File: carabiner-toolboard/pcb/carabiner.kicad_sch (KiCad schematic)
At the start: 24 parts, among them J1 MF-Vertical 43045-1612, J2 MF-Horizontal 43045-1621, J7 MF-Horizontal 43045-1600

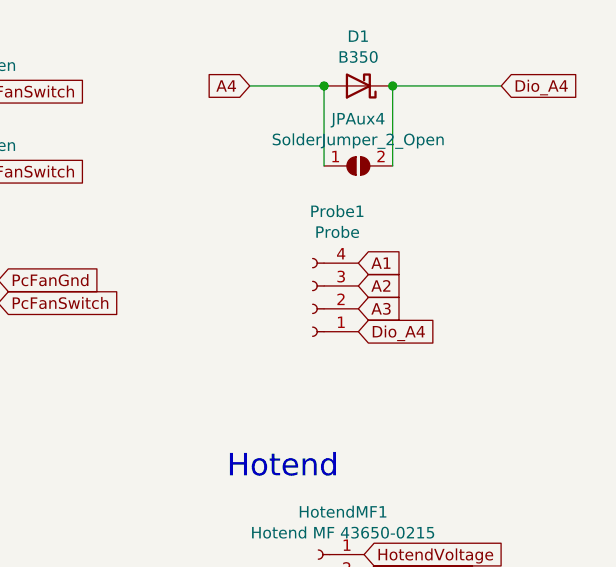
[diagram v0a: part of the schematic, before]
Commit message: Carabiner R1.1 - 'Who even needs more pins?'
Duplicates Aux3 - this allows you to wire up a BLTouch much easier
Increase the maximum ampere for PCFs to 2A total
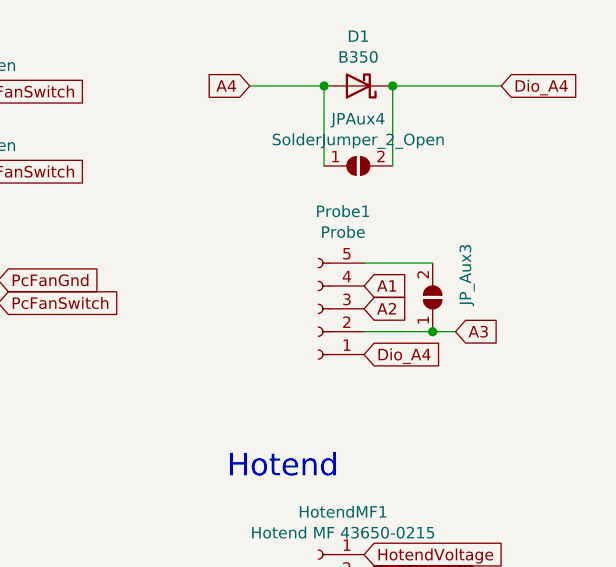
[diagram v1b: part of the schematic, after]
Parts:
- added JP_Aux3: SolderJumper_2_Open, Jumper:SolderJumper-2_P1.3mm_Open_TrianglePad1.0x1.5mm, symbol Jumper:SolderJumper_2_Open
- Probe1: footprint Connector_JST:JST_XH_B4B-XH-A_1x04_P2.50mm_Vertical -> Connector_JST:JST_XH_B5B-XH-A_1x05_P2.50mm_Vertical; symbol Connector:Conn_01x04_Female -> Connector:Conn_01x05_Female
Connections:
- net A3: now also JP_Aux3.1 (A)
- new net: JP_Aux3.2 (B), Probe1.5 (Pin_5)
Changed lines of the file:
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@@
   (junction (at 248.285 34.925) (diameter 1.016) (color 0 0 0 0))
   (junction (at 255.905 34.925) (diameter 1.016) (color 0 0 0 0))
+  (junction (at 260.35 62.23) (diameter 1.016) (color 0 0 0 0))
   (wire (pts (xy 196.85 56.515) (xy 200.66 56.515))
     (stroke (width 0) (type solid) (color 0 0 0 0))
@@
     (stroke (width 0) (type solid) (color 0 0 0 0))
   )
+  (wire (pts (xy 252.73 54.61) (xy 260.35 54.61))
+    (stroke (width 0) (type solid) (color 0 0 0 0))
+  )
+  (wire (pts (xy 252.73 62.23) (xy 260.35 62.23))
+    (stroke (width 0) (type solid) (color 0 0 0 0))
+  )
   (wire (pts (xy 255.905 34.925) (xy 255.905 43.815))
     (stroke (width 0) (type solid) (color 0 0 0 0))
   )
   (wire (pts (xy 255.905 34.925) (xy 267.97 34.925))
+    (stroke (width 0) (type solid) (color 0 0 0 0))
+  )
+  (wire (pts (xy 260.35 62.23) (xy 262.89 62.23))
     (stroke (width 0) (type solid) (color 0 0 0 0))
   )
@@
     )
   )
-  (global_label "A1" (shape input) (at 252.095 54.61 0) (fields_autoplaced)
-    (effects (font (size 1.27 1.27)) (justify left))
-    (property "Intersheet References" "${INTERSHEET_REFS}" (id 0) (at 256.8062 54.5306 0)
+  (global_label "A1" (shape input) (at 252.73 57.15 0) (fields_autoplaced)
+    (effects (font (size 1.27 1.27)) (justify left))
+    (property "Intersheet References" "${INTERSHEET_REFS}" (id 0) (at 257.4412 57.0706 0)
       (effects (font (size 1.27 1.27)) (justify left) hide)
     )
   )
-  (global_label "A2" (shape input) (at 252.095 57.15 0) (fields_autoplaced)
-    (effects (font (size 1.27 1.27)) (justify left))
-    (property "Intersheet References" "${INTERSHEET_REFS}" (id 0) (at 256.8062 57.0706 0)
+  (global_label "A2" (shape input) (at 252.73 59.69 0) (fields_autoplaced)
+    (effects (font (size 1.27 1.27)) (justify left))
+    (property "Intersheet References" "${INTERSHEET_REFS}" (id 0) (at 257.4412 59.6106 0)
       (effects (font (size 1.27 1.27)) (justify left) hide)
     )
   )
-  (global_label "A3" (shape input) (at 252.095 59.69 0) (fields_autoplaced)
-    (effects (font (size 1.27 1.27)) (justify left))
-    (property "Intersheet References" "${INTERSHEET_REFS}" (id 0) (at 256.8062 59.6106 0)
+  (global_label "Dio_A4" (shape input) (at 252.73 64.77 0) (fields_autoplaced)
+    (effects (font (size 1.27 1.27)) (justify left))
+    (property "Intersheet References" "${INTERSHEET_REFS}" (id 0) (at 261.4326 64.6906 0)
       (effects (font (size 1.27 1.27)) (justify left) hide)
     )
   )
-  (global_label "Dio_A4" (shape input) (at 252.095 62.23 0) (fields_autoplaced)
-    (effects (font (size 1.27 1.27)) (justify left))
-    (property "Intersheet References" "${INTERSHEET_REFS}" (id 0) (at 260.7976 62.1506 0)
+  (global_label "HotendVoltage" (shape input) (at 252.73 86.995 0) (fields_autoplaced)
+    (effects (font (size 1.27 1.27)) (justify left))
+    (property "Intersheet References" "${INTERSHEET_REFS}" (id 0) (at 0 0 0)
+      (effects (font (size 1.27 1.27)) hide)
+    )
+  )
+  (global_label "HotendNeg" (shape input) (at 252.73 89.535 0) (fields_autoplaced)
+    (effects (font (size 1.27 1.27)) (justify left))
+    (property "Intersheet References" "${INTERSHEET_REFS}" (id 0) (at 0 0 0)
+      (effects (font (size 1.27 1.27)) hide)
+    )
+  )
+  (global_label "HotendVoltage" (shape input) (at 252.73 99.695 0) (fields_autoplaced)
+    (effects (font (size 1.27 1.27)) (justify left))
+    (property "Intersheet References" "${INTERSHEET_REFS}" (id 0) (at 0 0 0)
+      (effects (font (size 1.27 1.27)) hide)
+    )
+  )
+  (global_label "HotendNeg" (shape input) (at 252.73 102.235 0) (fields_autoplaced)
+    (effects (font (size 1.27 1.27)) (justify left))
+    (property "Intersheet References" "${INTERSHEET_REFS}" (id 0) (at 0 0 0)
+      (effects (font (size 1.27 1.27)) hide)
+    )
+  )
+  (global_label "HotendVoltage" (shape input) (at 252.73 111.125 0) (fields_autoplaced)
+    (effects (font (size 1.27 1.27)) (justify left))
+    (property "Intersheet References" "${INTERSHEET_REFS}" (id 0) (at 0 0 0)
+      (effects (font (size 1.27 1.27)) hide)
+    )
+  )
+  (global_label "HotendNeg" (shape input) (at 252.73 113.665 0) (fields_autoplaced)
+    (effects (font (size 1.27 1.27)) (justify left))
+    (property "Intersheet References" "${INTERSHEET_REFS}" (id 0) (at 0 0 0)
+      (effects (font (size 1.27 1.27)) hide)
+    )
+  )
+  (global_label "A3" (shape input) (at 262.89 62.23 0) (fields_autoplaced)
+    (effects (font (size 1.27 1.27)) (justify left))
+    (property "Intersheet References" "${INTERSHEET_REFS}" (id 0) (at 267.6012 62.1506 0)
       (effects (font (size 1.27 1.27)) (justify left) hide)
-    )
-  )
-  (global_label "HotendVoltage" (shape input) (at 252.73 86.995 0) (fields_autoplaced)
-    (effects (font (size 1.27 1.27)) (justify left))
-    (property "Intersheet References" "${INTERSHEET_REFS}" (id 0) (at 0 0 0)
-      (effects (font (size 1.27 1.27)) hide)
-    )
-  )
-  (global_label "HotendNeg" (shape input) (at 252.73 89.535 0) (fields_autoplaced)
-    (effects (font (size 1.27 1.27)) (justify left))
-    (property "Intersheet References" "${INTERSHEET_REFS}" (id 0) (at 0 0 0)
-      (effects (font (size 1.27 1.27)) hide)
-    )
-  )
-  (global_label "HotendVoltage" (shape input) (at 252.73 99.695 0) (fields_autoplaced)
-    (effects (font (size 1.27 1.27)) (justify left))
-    (property "Intersheet References" "${INTERSHEET_REFS}" (id 0) (at 0 0 0)
-      (effects (font (size 1.27 1.27)) hide)
-    )
-  )
-  (global_label "HotendNeg" (shape input) (at 252.73 102.235 0) (fields_autoplaced)
-    (effects (font (size 1.27 1.27)) (justify left))
-    (property "Intersheet References" "${INTERSHEET_REFS}" (id 0) (at 0 0 0)
-      (effects (font (size 1.27 1.27)) hide)
-    )
-  )
-  (global_label "HotendVoltage" (shape input) (at 252.73 111.125 0) (fields_autoplaced)
-    (effects (font (size 1.27 1.27)) (justify left))
-    (property "Intersheet References" "${INTERSHEET_REFS}" (id 0) (at 0 0 0)
-      (effects (font (size 1.27 1.27)) hide)
-    )
-  )
-  (global_label "HotendNeg" (shape input) (at 252.73 113.665 0) (fields_autoplaced)
-    (effects (font (size 1.27 1.27)) (justify left))
-    (property "Intersheet References" "${INTERSHEET_REFS}" (id 0) (at 0 0 0)
-      (effects (font (size 1.27 1.27)) hide)
     )
   )
@@
     (pin "2")
   )
+  (symbol (lib_id "Jumper:SolderJumper_2_Open") (at 260.35 58.42 90) (unit 1)
+    (in_bom yes) (on_board yes)
+    (property "Reference" "JP_Aux3" (id 0) (at 264.033 55.88 0))
+    (property "Value" "SolderJumper_2_Open" (id 1) (at 257.4544 58.42 0)
+      (effects (font (size 1.27 1.27)) hide)
+    )
+    (property "Footprint" "Jumper:SolderJumper-2_P1.3mm_Open_TrianglePad1.0x1.5mm" (id 2) (at 260.35 58.42 0)
+      (effects (font (size 1.27 1.27)) hide)
+    )
+    (property "Datasheet" "~" (id 3) (at 260.35 58.42 0)
+      (effects (font (size 1.27 1.27)) hide)
+    )
+    (pin "1")
+    (pin "2")
+  )
   (symbol (lib_id "Connector:Conn_01x02_Female") (at 47.625 37.465 180) (unit 1)
     (in_bom yes) (on_board yes)
@@
     (pin "4")
   )
-  (symbol (lib_id "Connector:Conn_01x04_Female") (at 247.015 59.69 180) (unit 1)
-    (in_bom yes) (on_board yes)
-    (property "Reference" "Probe1" (id 0) (at 249.7582 48.895 0))
-    (property "Value" "Probe" (id 1) (at 249.7582 51.2064 0))
-    (property "Footprint" "Connector_JST:JST_XH_B4B-XH-A_1x04_P2.50mm_Vertical" (id 2) (at 247.015 59.69 0)
-      (effects (font (size 1.27 1.27)) hide)
-    )
-    (property "Datasheet" "~" (id 3) (at 247.015 59.69 0)
+  (symbol (lib_id "Connector:Conn_01x05_Female") (at 247.65 59.69 180) (unit 1)
+    (in_bom yes) (on_board yes)
+    (property "Reference" "Probe1" (id 0) (at 250.3932 48.895 0))
+    (property "Value" "Probe" (id 1) (at 250.3932 51.2064 0))
+    (property "Footprint" "Connector_JST:JST_XH_B5B-XH-A_1x05_P2.50mm_Vertical" (id 2) (at 247.65 59.69 0)
+      (effects (font (size 1.27 1.27)) hide)
+    )
+    (property "Datasheet" "~" (id 3) (at 247.65 59.69 0)
       (effects (font (size 1.27 1.27)) hide)
     )
@@
     (pin "3")
     (pin "4")
+    (pin "5")
   )
   (symbol (lib_id "Graphic:Logo_Open_Hardware_Small") (at 151.13 99.06 0) (unit 1)
@@
       (reference "JPAux4") (unit 1) (value "SolderJumper_2_Open") (footprint "Jumper:SolderJumper-2_P1.3mm_Open_TrianglePad1.0x1.5mm")
     )
+    (path "/5ccb0dab-e449-450f-be0b-c1fca9d3638a"
+      (reference "JP_Aux3") (unit 1) (value "SolderJumper_2_Open") (footprint "Jumper:SolderJumper-2_P1.3mm_Open_TrianglePad1.0x1.5mm")
+    )
     (path "/00000000-0000-0000-0000-00005ff3998e"
       (reference "JP_HEF_Alt1") (unit 1) (value "SolderJumper_2_Open") (footprint "Jumper:SolderJumper-2_P1.3mm_Open_TrianglePad1.0x1.5mm")
@@
     )
     (path "/00000000-0000-0000-0000-00005ee118e3"
-      (reference "Probe1") (unit 1) (value "Probe") (footprint "Connector_JST:JST_XH_B4B-XH-A_1x04_P2.50mm_Vertical")
+      (reference "Probe1") (unit 1) (value "Probe") (footprint "Connector_JST:JST_XH_B5B-XH-A_1x05_P2.50mm_Vertical")
     )
     (path "/00000000-0000-0000-0000-00005ee148c5"

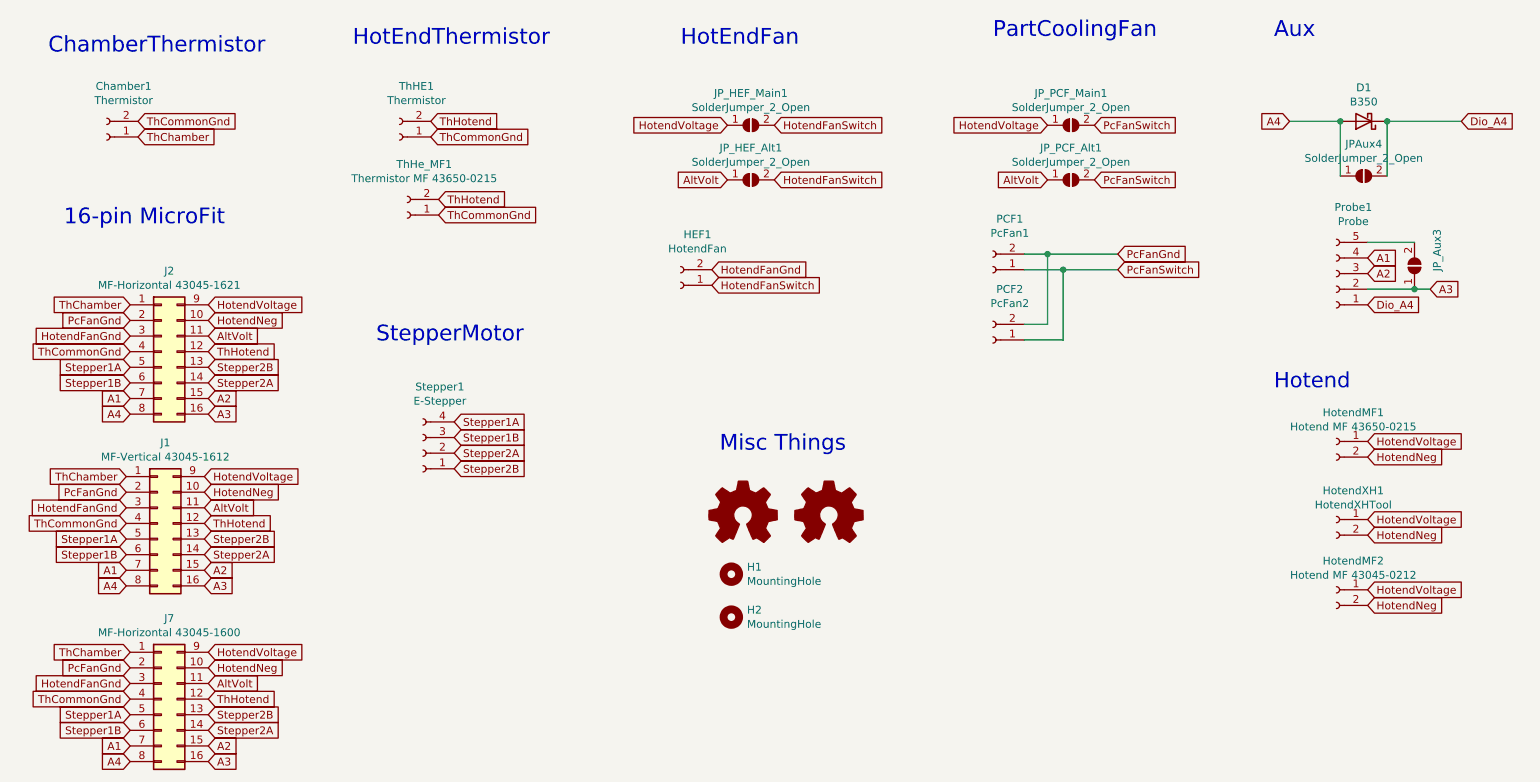
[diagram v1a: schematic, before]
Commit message: Carabiner R 1.2 - Polishing it
- Renaming ports to fit the new unified naming scheme.
- Updated Readme to reflect that
- Support USB with the Aux ports! Use A2 and A3 for D+/D-
- Rework the motor trace routing
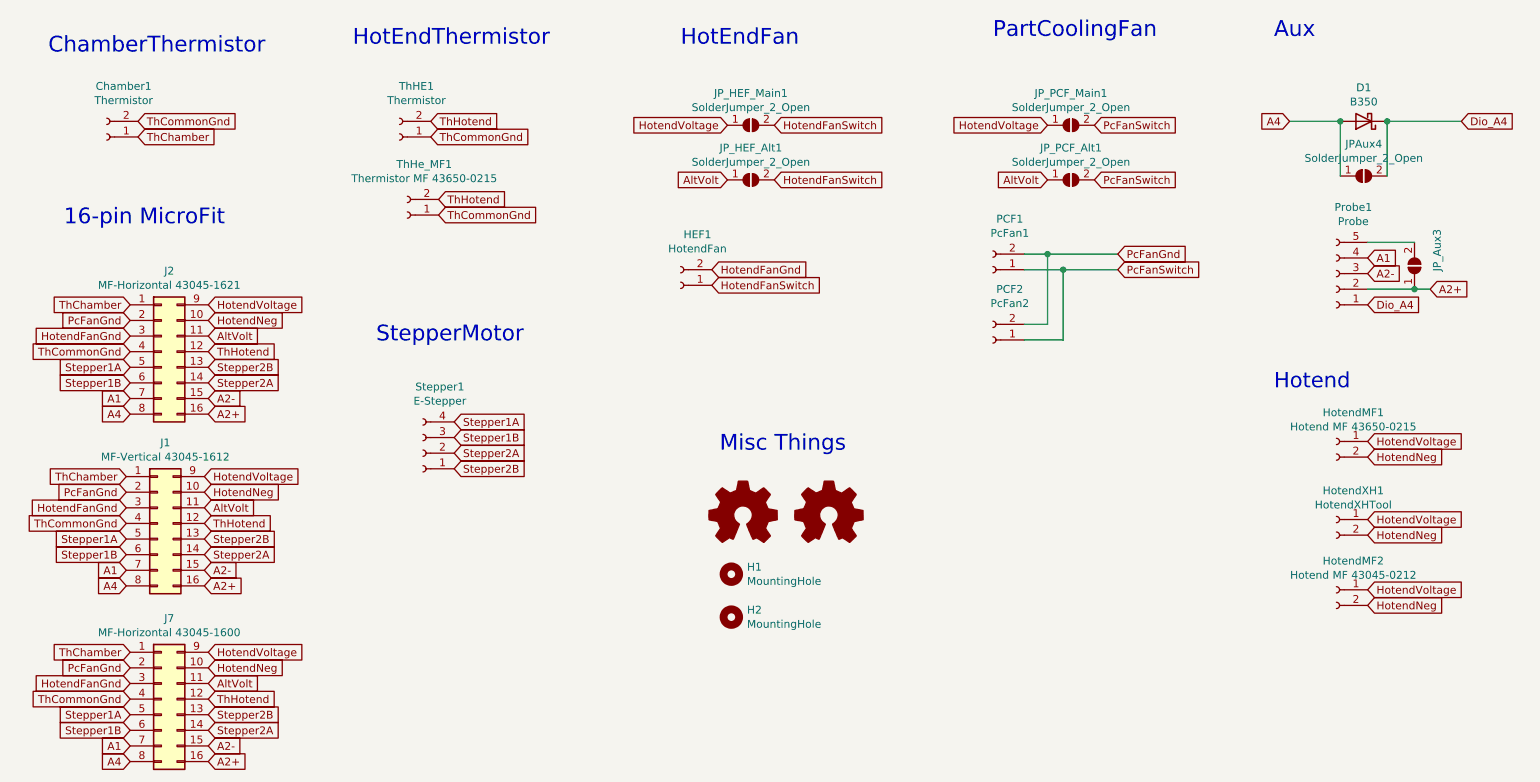
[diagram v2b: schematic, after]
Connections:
- net A2 renamed A2-
- net A3 renamed A2+
